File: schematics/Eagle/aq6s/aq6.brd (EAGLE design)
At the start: 100 x 80 mm, 5 parts

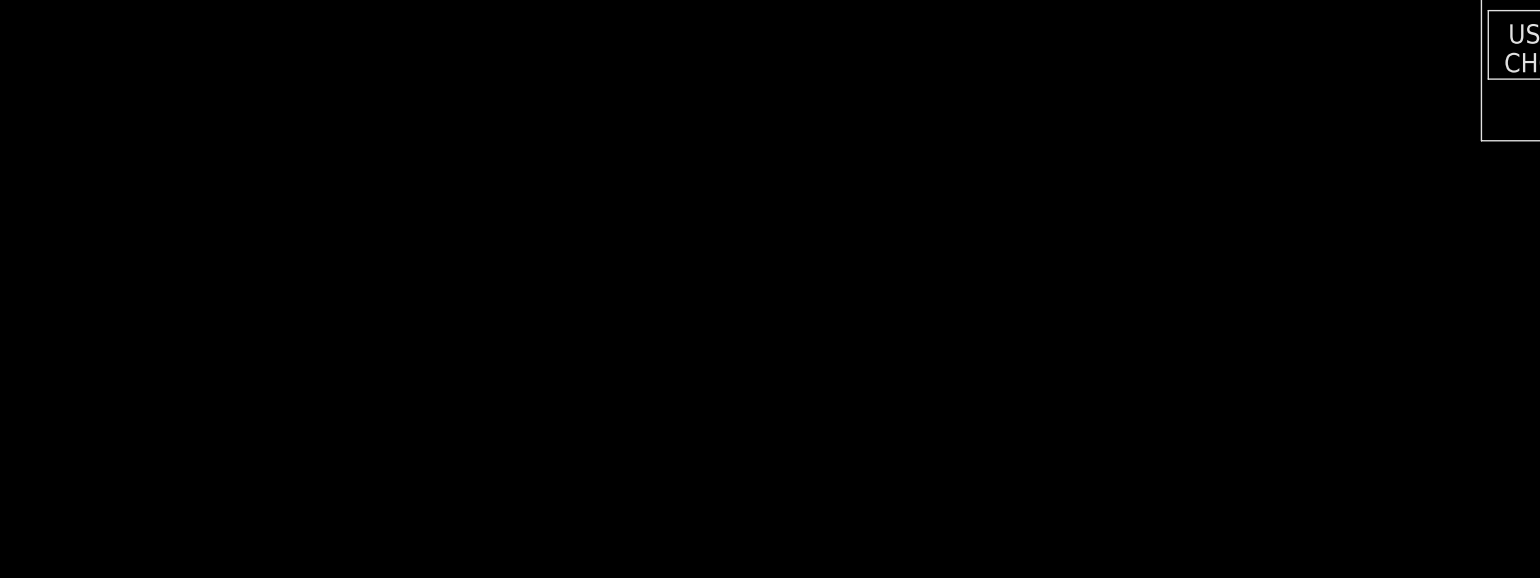
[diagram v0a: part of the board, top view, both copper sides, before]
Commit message: Added more components to Eagle schematic, library
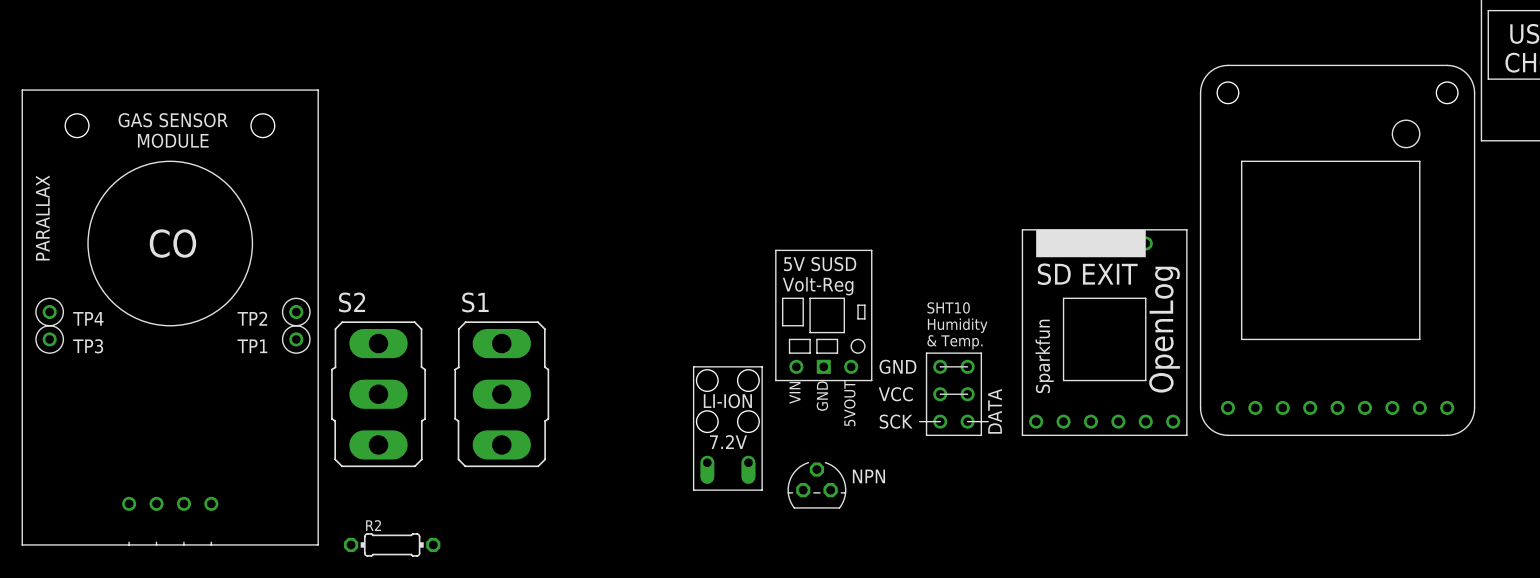
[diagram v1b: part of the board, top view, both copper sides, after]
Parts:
- added CO: CO, air_quality_parts:GSM_PARALLAX
- added LI-ION: 7.2V, air_quality_parts:BATTERY_WITH_WIRE_HOLES
- added NPN: S9014, transistor:TO92-E1
- added R2: 10KΩ, resistor:0204/7
- added S1, S2: (no value), switch:M9040P
- added U$4: ADAFRUIT_GPS_V3, air_quality_parts:ADAFRUIT_GPS_V3
- added U$5: SPARKFUN_OPENLOG, air_quality_parts:SPARKFUN_OPENLOG
- added U$6: DFR_TEMP_HUMIDITY, air_quality_parts:DFR_TEMP_HUMIDITY
- added U$7: 5V_SUSD_VOLT_REG, air_quality_parts:5V_SUSD_VOLT_REG
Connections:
- new net N$10: S2.2, U$2.-SW
- new net N$11: LI-ION.VCC, S1.2
- new net N$12: U$2.D13, U$6.SCK
- new net N$13: U$2.D11*, U$6.DATA
- new net N$14: S1.3, U$7.VIN
- new net N$15: LI-ION.GND, U$7.GND
- new net N$16: NPN.2, R2.1
- new net N$17: R2.2, U$2.D5*
- new net N$18: CO.+5V, U$7.VOUT
- new net N$19: CO.HSW
- new net N$20: CO.P$1, U$2.A7
- new net N$4: U$2.D3*, U$4.RX
- new net N$5: U$2.D2, U$4.TX
- new net N$6: S2.3, U$2.+SW
- new net N$7: U$2.D8
- new net N$8: U$2.D7
- new net N$9: U$2.D6*, U$5.TXO
- net 3V3: now also U$2.3V3, U$4.VIN, U$5.VCC, U$6.VCC, U$6.VCC@2; no longer U$2.P$1
- net GND: now also CO.GND, NPN.3, U$2.GND, U$4.GND, U$5.GND, U$6.GND, U$6.GND@2
- net N$1: now also U$2.D12; no longer U$2.P$13
- net N$3: now also U$2.A6; no longer U$2.P$27
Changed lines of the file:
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@@
 <element name="R1" library="resistor" package="0204/7" value="150Ω" x="81.28" y="38.1"/>
 <element name="U$3" library="air_quality_parts" package="POLOLU_VAR_VOLTAGE_REG" value="POLOLU_VAR_VOLTAGE_REG" x="81.28" y="50.8"/>
+<element name="U$4" library="air_quality_parts" package="ADAFRUIT_GPS_V3" value="ADAFRUIT_GPS_V3" x="-46.99" y="1.27"/>
+<element name="U$5" library="air_quality_parts" package="SPARKFUN_OPENLOG" value="SPARKFUN_OPENLOG" x="-63.5" y="1.27"/>
+<element name="U$6" library="air_quality_parts" package="DFR_TEMP_HUMIDITY" value="DFR_TEMP_HUMIDITY" x="-69.85" y="5.08"/>
+<element name="U$7" library="air_quality_parts" package="5V_SUSD_VOLT_REG" value="5V_SUSD_VOLT_REG" x="-82.55" y="12.7"/>
+<element name="NPN" library="transistor" package="TO92-E1" value="S9014" x="-82.55" y="-3.81"/>
+<element name="LI-ION" library="air_quality_parts" package="BATTERY_WITH_WIRE_HOLES" value="7.2V" x="-93.98" y="-3.81"/>
+<element name="S1" library="switch" package="M9040P" value="" x="-111.76" y="5.08"/>
+<element name="S2" library="switch" package="M9040P" value="" x="-123.19" y="5.08"/>
+<element name="R2" library="resistor" package="0204/7" value="10KΩ" x="-121.92" y="-8.89"/>
+<element name="CO" library="air_quality_parts" package="GSM_PARALLAX" value="CO" x="-156.21" y="-8.89"/>
 </elements>
 <signals>
 <signal name="GND">
 <contactref element="U$1" pad="P$2"/>
+<contactref element="U$1" pad="P$4"/>
 <contactref element="C1" pad="2"/>
 <contactref element="U$3" pad="P$3"/>
-<contactref element="U$1" pad="P$4"/>
-<wire x1="82.55" y1="33.02" x2="82.55" y2="44.45" width="0" layer="19" extent="1-1"/>
+<contactref element="U$6" pad="GND"/>
+<contactref element="U$6" pad="GND@2"/>
+<contactref element="U$2" pad="GND"/>
+<contactref element="U$4" pad="GND"/>
+<contactref element="U$5" pad="GND"/>
+<contactref element="NPN" pad="3"/>
+<contactref element="CO" pad="GND"/>
+<wire x1="-81.28" y1="-3.81" x2="-138.684" y2="-5.08" width="0" layer="19" extent="1-1"/>
+<wire x1="-71.12" y1="7.62" x2="-81.28" y2="-3.81" width="0" layer="19" extent="1-1"/>
+<wire x1="-68.58" y1="7.62" x2="-71.12" y2="7.62" width="0" layer="19" extent="1-1"/>
+<wire x1="-52.07" y1="2.54" x2="-68.58" y2="7.62" width="0" layer="19" extent="1-1"/>
+<wire x1="-29.21" y1="3.81" x2="-52.07" y2="2.54" width="0" layer="19" extent="1-1"/>
+<wire x1="12.7" y1="30.48" x2="-29.21" y2="3.81" width="0" layer="19" extent="1-1"/>
+<wire x1="82.55" y1="33.02" x2="12.7" y2="30.48" width="0" layer="19" extent="1-1"/>
 <wire x1="88.9" y1="33.02" x2="82.55" y2="33.02" width="0" layer="19" extent="1-1"/>
 <wire x1="88.9" y1="27.94" x2="88.9" y2="33.02" width="0" layer="19" extent="1-1"/>
-</signal>
-<signal name="N$1">
-<contactref element="U$1" pad="P$3"/>
-<contactref element="U$2" pad="P$13"/>
-<wire x1="40.64" y1="30.48" x2="88.9" y2="30.48" width="0" layer="19" extent="1-1"/>
+<wire x1="82.55" y1="44.45" x2="82.55" y2="33.02" width="0" layer="19" extent="1-1"/>
 </signal>
 <signal name="5V">
+<contactref element="U$1" pad="P$6"/>
 <contactref element="U$3" pad="P$4"/>
 <contactref element="R1" pad="2"/>
-<contactref element="U$1" pad="P$6"/>
 <wire x1="85.09" y1="38.1" x2="85.09" y2="44.45" width="0" layer="19" extent="1-1"/>
 <wire x1="88.9" y1="22.86" x2="85.09" y2="38.1" width="0" layer="19" extent="1-1"/>
 </signal>
 <signal name="N$2">
-<contactref element="C1" pad="1"/>
 <contactref element="R1" pad="1"/>
 <contactref element="U$1" pad="P$1"/>
-<wire x1="77.47" y1="38.1" x2="77.47" y2="33.02" width="0" layer="19" extent="1-1"/>
-<wire x1="88.9" y1="35.56" x2="77.47" y2="38.1" width="0" layer="19" extent="1-1"/>
+<contactref element="C1" pad="1"/>
+<wire x1="77.47" y1="38.1" x2="88.9" y2="35.56" width="0" layer="19" extent="1-1"/>
+<wire x1="77.47" y1="33.02" x2="77.47" y2="38.1" width="0" layer="19" extent="1-1"/>
+</signal>
+<signal name="N$1">
+<contactref element="U$1" pad="P$3"/>
+<contactref element="U$2" pad="D12"/>
+<wire x1="40.64" y1="30.48" x2="88.9" y2="30.48" width="0" layer="19" extent="1-1"/>
+</signal>
+<signal name="3V3">
+<contactref element="U$2" pad="3V3"/>
+<contactref element="U$3" pad="P$2"/>
+<contactref element="U$4" pad="VIN"/>
+<contactref element="U$5" pad="VCC"/>
+<contactref element="U$6" pad="VCC@2"/>
+<contactref element="U$6" pad="VCC"/>
+<wire x1="10.16" y1="30.48" x2="80.01" y2="44.45" width="0" layer="19" extent="1-1"/>
+<wire x1="-26.67" y1="3.81" x2="10.16" y2="30.48" width="0" layer="19" extent="1-1"/>
+<wire x1="-54.61" y1="2.54" x2="-26.67" y2="3.81" width="0" layer="19" extent="1-1"/>
+<wire x1="-68.58" y1="5.08" x2="-54.61" y2="2.54" width="0" layer="19" extent="1-1"/>
+<wire x1="-71.12" y1="5.08" x2="-68.58" y2="5.08" width="0" layer="19" extent="1-1"/>
 </signal>
 <signal name="N$3">
 <contactref element="U$1" pad="P$5"/>
-<contactref element="U$2" pad="P$27"/>
+<contactref element="U$2" pad="A6"/>
 <wire x1="40.64" y1="53.34" x2="88.9" y2="25.4" width="0" layer="19" extent="1-1"/>
 </signal>
-<signal name="3V3">
-<contactref element="U$3" pad="P$2"/>
-<contactref element="U$2" pad="P$1"/>
-<wire x1="10.16" y1="30.48" x2="80.01" y2="44.45" width="0" layer="19" extent="1-1"/>
+<signal name="N$4">
+<contactref element="U$4" pad="RX"/>
+<contactref element="U$2" pad="D3*"/>
+<wire x1="-31.75" y1="3.81" x2="17.78" y2="30.48" width="0" layer="19" extent="1-1"/>
+</signal>
+<signal name="N$5">
+<contactref element="U$4" pad="TX"/>
+<contactref element="U$2" pad="D2"/>
+<wire x1="-34.29" y1="3.81" x2="15.24" y2="30.48" width="0" layer="19" extent="1-1"/>
+</signal>
+<signal name="N$7">
+<contactref element="U$2" pad="D8"/>
+</signal>
+<signal name="N$9">
+<contactref element="U$5" pad="TXO"/>
+<contactref element="U$2" pad="D6*"/>
+<wire x1="-57.15" y1="2.54" x2="25.4" y2="30.48" width="0" layer="19" extent="1-1"/>
+</signal>
+<signal name="N$8">
+<contactref element="U$2" pad="D7"/>
+</signal>
+<signal name="N$12">
+<contactref element="U$6" pad="SCK"/>
+<contactref element="U$2" pad="D13"/>
+<wire x1="-71.12" y1="2.54" x2="43.18" y2="30.48" width="0" layer="19" extent="1-1"/>
+</signal>
+<signal name="N$13">
+<contactref element="U$6" pad="DATA"/>
+<contactref element="U$2" pad="D11*"/>
+<wire x1="-68.58" y1="2.54" x2="38.1" y2="30.48" width="0" layer="19" extent="1-1"/>
+</signal>
+<signal name="N$6">
+<contactref element="S2" pad="3"/>
+<contactref element="U$2" pad="+SW"/>
+<wire x1="2.54" y1="45.72" x2="-123.19" y2="0.381" width="0" layer="19" extent="1-1"/>
+</signal>
+<signal name="N$10">
+<contactref element="S2" pad="2"/>
+<contactref element="U$2" pad="-SW"/>
+<wire x1="5.08" y1="45.72" x2="-123.19" y2="5.08" width="0" layer="19" extent="1-1"/>
+</signal>
+<signal name="N$11">
+<contactref element="S1" pad="2"/>
+<contactref element="LI-ION" pad="VCC"/>
+<wire x1="-88.9" y1="-1.27" x2="-111.76" y2="5.08" width="0" layer="19" extent="1-1"/>
+</signal>
+<signal name="N$14">
+<contactref element="S1" pad="3"/>
+<contactref element="U$7" pad="VIN"/>
+<wire x1="-84.455" y1="7.62" x2="-111.76" y2="0.381" width="0" layer="19" extent="1-1"/>
+</signal>
+<signal name="N$15">
+<contactref element="U$7" pad="GND"/>
+<contactref element="LI-ION" pad="GND"/>
+<wire x1="-81.915" y1="7.62" x2="-92.71" y2="-1.27" width="0" layer="19" extent="1-1"/>
+</signal>
+<signal name="N$16">
+<contactref element="R2" pad="1"/>
+<contactref element="NPN" pad="2"/>
+<wire x1="-82.55" y1="-1.905" x2="-125.73" y2="-8.89" width="0" layer="19" extent="1-1"/>
+</signal>
+<signal name="N$17">
+<contactref element="R2" pad="2"/>
+<contactref element="U$2" pad="D5*"/>
+<wire x1="22.86" y1="30.48" x2="-118.11" y2="-8.89" width="0" layer="19" extent="1-1"/>
+</signal>
+<signal name="N$18">
+<contactref element="U$7" pad="VOUT"/>
+<contactref element="CO" pad="+5V"/>
+<wire x1="-79.375" y1="7.62" x2="-141.224" y2="-5.08" width="0" layer="19" extent="1-1"/>
+</signal>
+<signal name="N$19">
+<contactref element="CO" pad="HSW"/>
+</signal>
+<signal name="N$20">
+<contactref element="CO" pad="P$1"/>
+<contactref element="U$2" pad="A7"/>
+<wire x1="43.18" y1="53.34" x2="-153.67" y2="12.7" width="0" layer="19" extent="1-1"/>
 </signal>
 </signals>

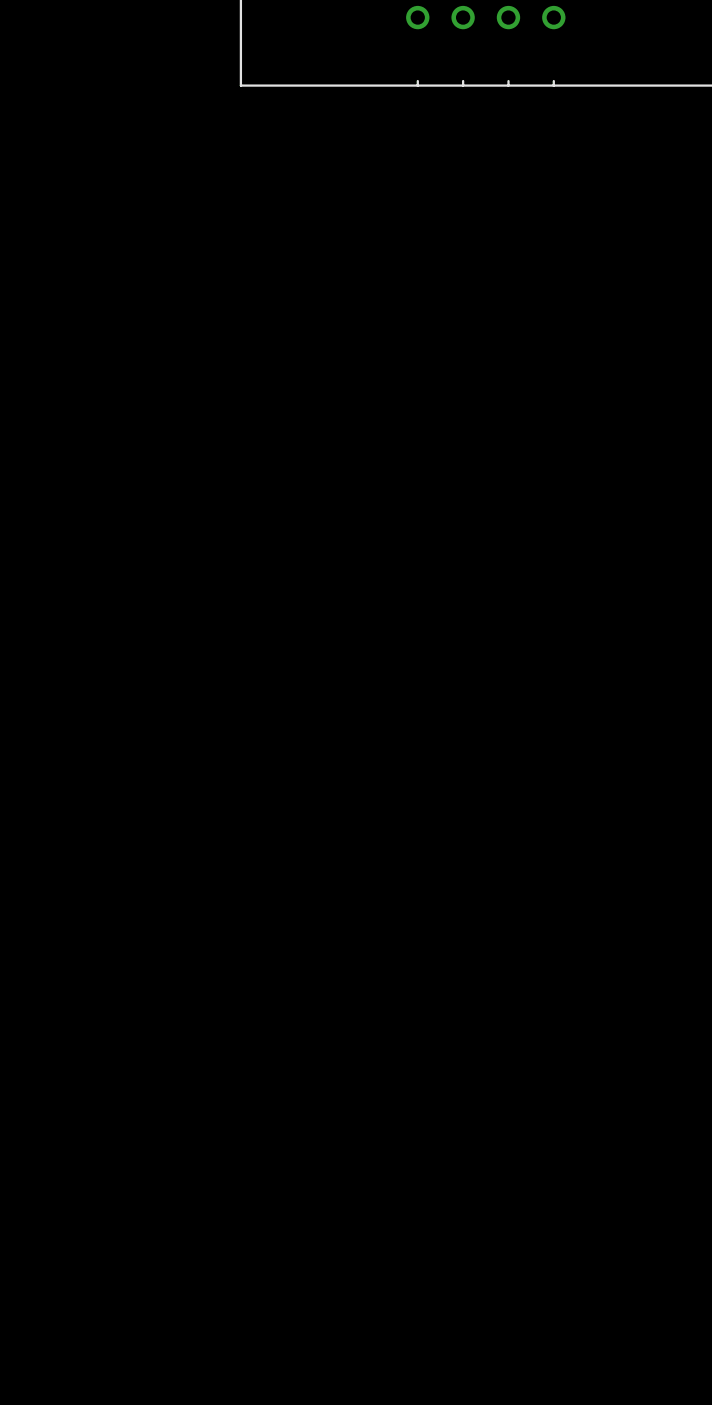
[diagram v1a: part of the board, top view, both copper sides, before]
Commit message: Finished circuit diagram, needs checking
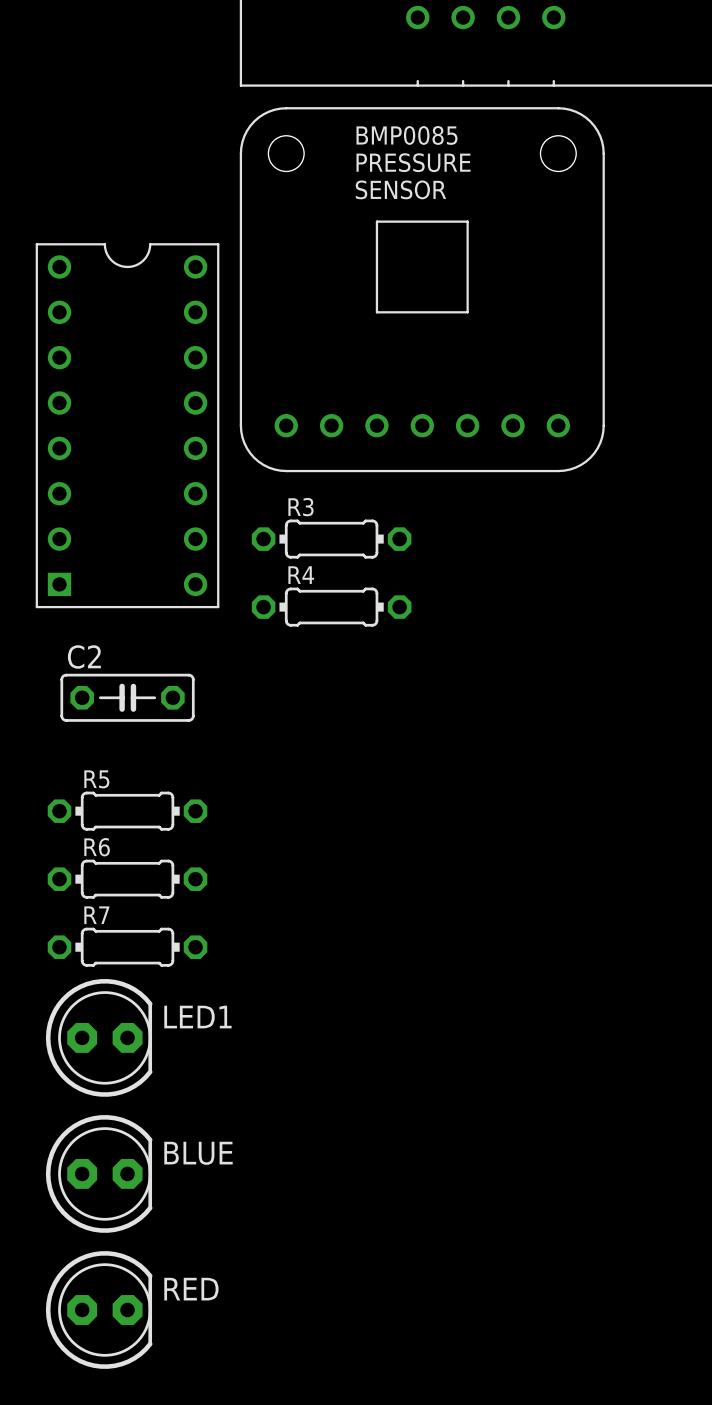
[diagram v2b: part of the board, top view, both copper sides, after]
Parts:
- added BLUE, RED: (no value), adafruit:LED5MM
- added C2: 1 uF, resistor:C050-025X075
- added LED1: GRN, adafruit:LED5MM
- added R3: 10KΩ, resistor:0204/7
- added R4: 4.7kΩ, resistor:0204/7
- added R5, R6, R7: 220Ω, resistor:0204/7
- added U$8: BMP085, air_quality_parts:BMP085
- added U$9: M74HC595B1, air_quality_parts:16DIP
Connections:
- new net 3VO: U$8.3VO
- new net N$21: R3.2, R4.2, U$2.A1
- new net N$22: U$2.A2, U$9.P$14
- new net N$23: U$2.A5, U$8.SCL
- new net N$24: U$2.A4, U$8.SDA
- new net N$25: R5.2, U$9.P$15
- new net N$26: U$2.D9*, U$9.P$11
- new net N$27: U$2.D10, U$9.P$12
- new net N$28: R7.2, U$9.P$2
- new net N$29: R6.2, U$9.P$1
- new net N$30: R7.1, RED.A
- new net N$31: BLUE.A, R6.1
- new net N$32: LED1.A, R5.1
- net 3V3: now also C2.2, U$8.VIN, U$9.P$10, U$9.P$16
- net GND: now also BLUE.K, C2.1, LED1.K, R4.1, RED.K, U$8.GND
- net N$18: now also R3.1

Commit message: PCB layout tentatively ok, routing next
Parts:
- removed LED1: GRN, adafruit:LED5MM
- removed NPN: S9014, transistor:TO92-E1
- removed S1, S2: (no value), switch:M9040P
- added GRN: (no value), adafruit:LED5MM
- added U$10, U$11: SWITCH, air_quality_parts:SWITCH
- added U$12: NPN, air_quality_parts:NPN
- moved RED 261.8 mm to (69.2, 41.9), turned to 180 degrees
- moved BLUE 257.1 mm to (69.2, 38.7), turned to 180 degrees
- moved U$8 247.8 mm to (79.4, 46.4)
- moved R7 245.2 mm to (70.5, 19.1), turned to 270 degrees
- moved R6 242.2 mm to (68.6, 19.1), turned to 270 degrees
- moved R5 239.3 mm to (66.7, 19.1), turned to 270 degrees
- moved C2 236.4 mm to (67.3, 12.1), turned to 180 degrees
- moved CO 228.4 mm to (72.0, 0.51)
- moved R4 224.0 mm to (68.6, 5.71), turned to 90 degrees
- moved R3 220.8 mm to (66.0, 5.71), turned to 90 degrees
- moved U$9 215.6 mm to (51.4, 8.26), turned to 90 degrees
- moved R2 192.5 mm to (66.7, 29.8), turned to 90 degrees
- moved U$6 116.7 mm to (40.8, 42.4), turned to 90 degrees
- moved U$5 109.3 mm to (35.7, 47.2)
- moved LI-ION 107.1 mm to (12.7, 5.59), turned to 90 degrees
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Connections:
- net GND: now also GRN.K, U$12.E; no longer LED1.K, NPN.3
- net N$10: now also U$10.P$2; no longer S2.2
- net N$11: now also U$11.P$2; no longer S1.2
- net N$14: now also U$11.P$1; no longer S1.3
- net N$16: now also U$12.B; no longer NPN.2
- net N$19: now also U$12.C
- net N$20: now also CO.TP1; no longer CO.P$1
- net N$32: now also GRN.A; no longer LED1.A
- net N$6: now also U$10.P$1; no longer S2.3
- net N$7: now also U$5.GRN
- net N$8: now also U$5.RXI
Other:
- board size 100 x 80 mm -> 99.8 x 66.8 mm
